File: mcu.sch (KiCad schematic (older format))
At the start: 13 parts, among them P3 SWD, P7 Thumb-Joystick, SW1 SW_PUSH, U3 LCD-2x16, U4 STM32F401xB/C-LQFP

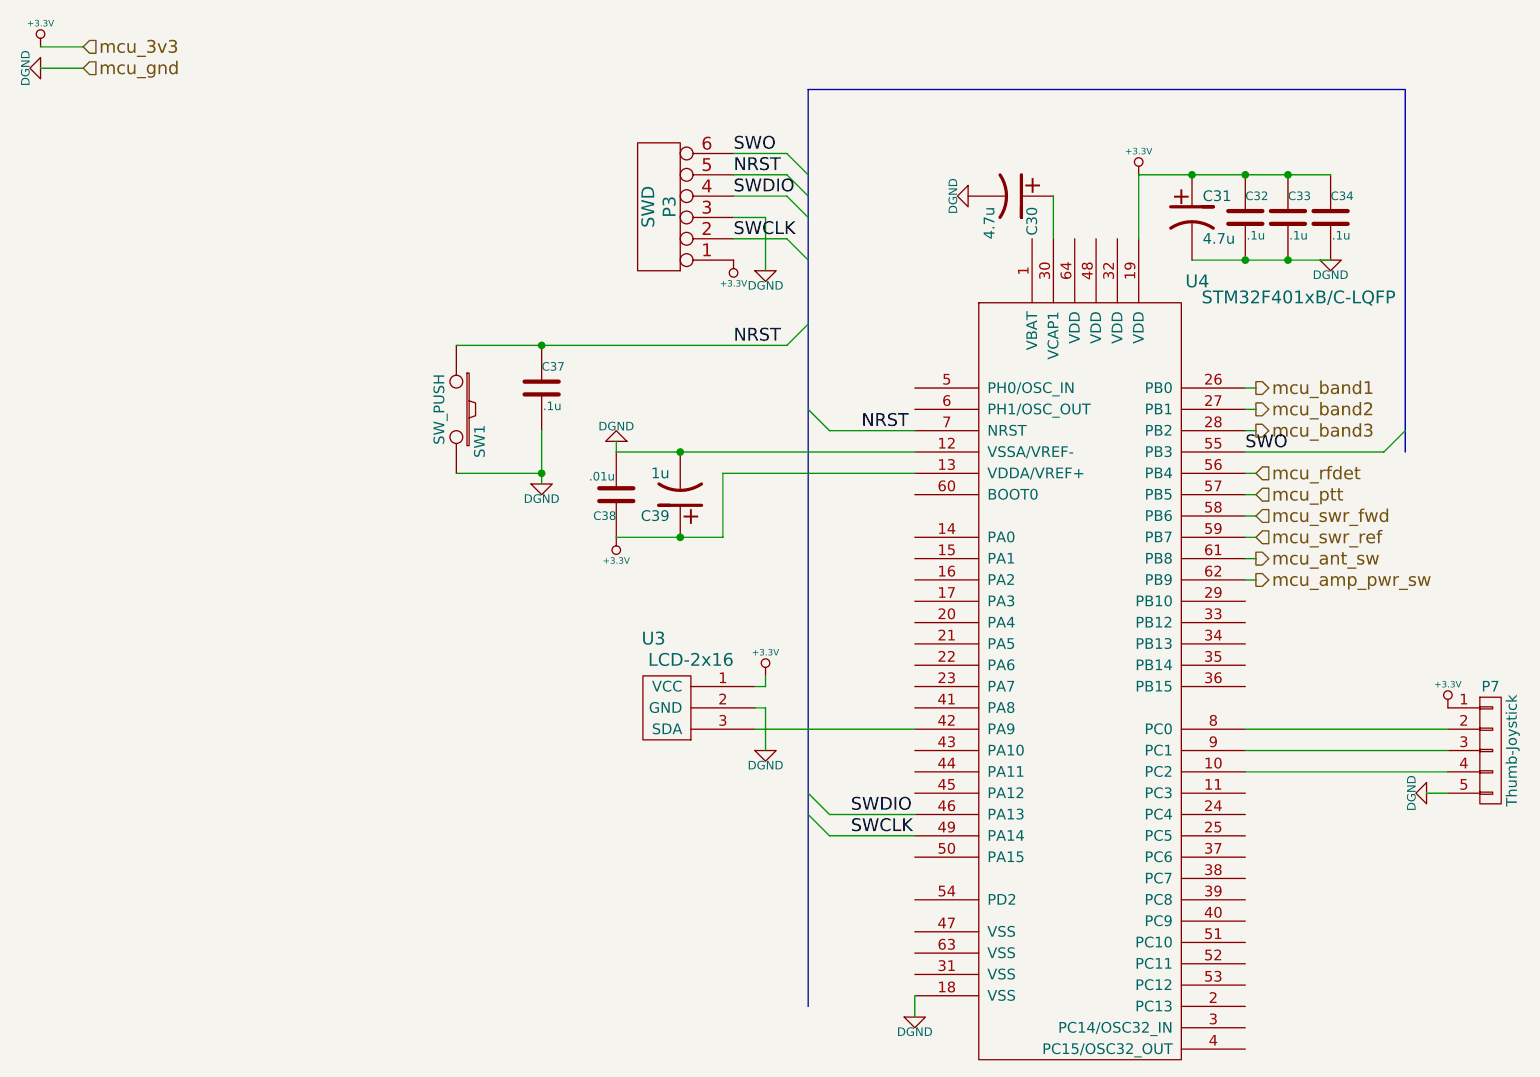
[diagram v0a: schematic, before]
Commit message: All layed out
Several net errors fixed, and some mcu pins reassigned for better layout.
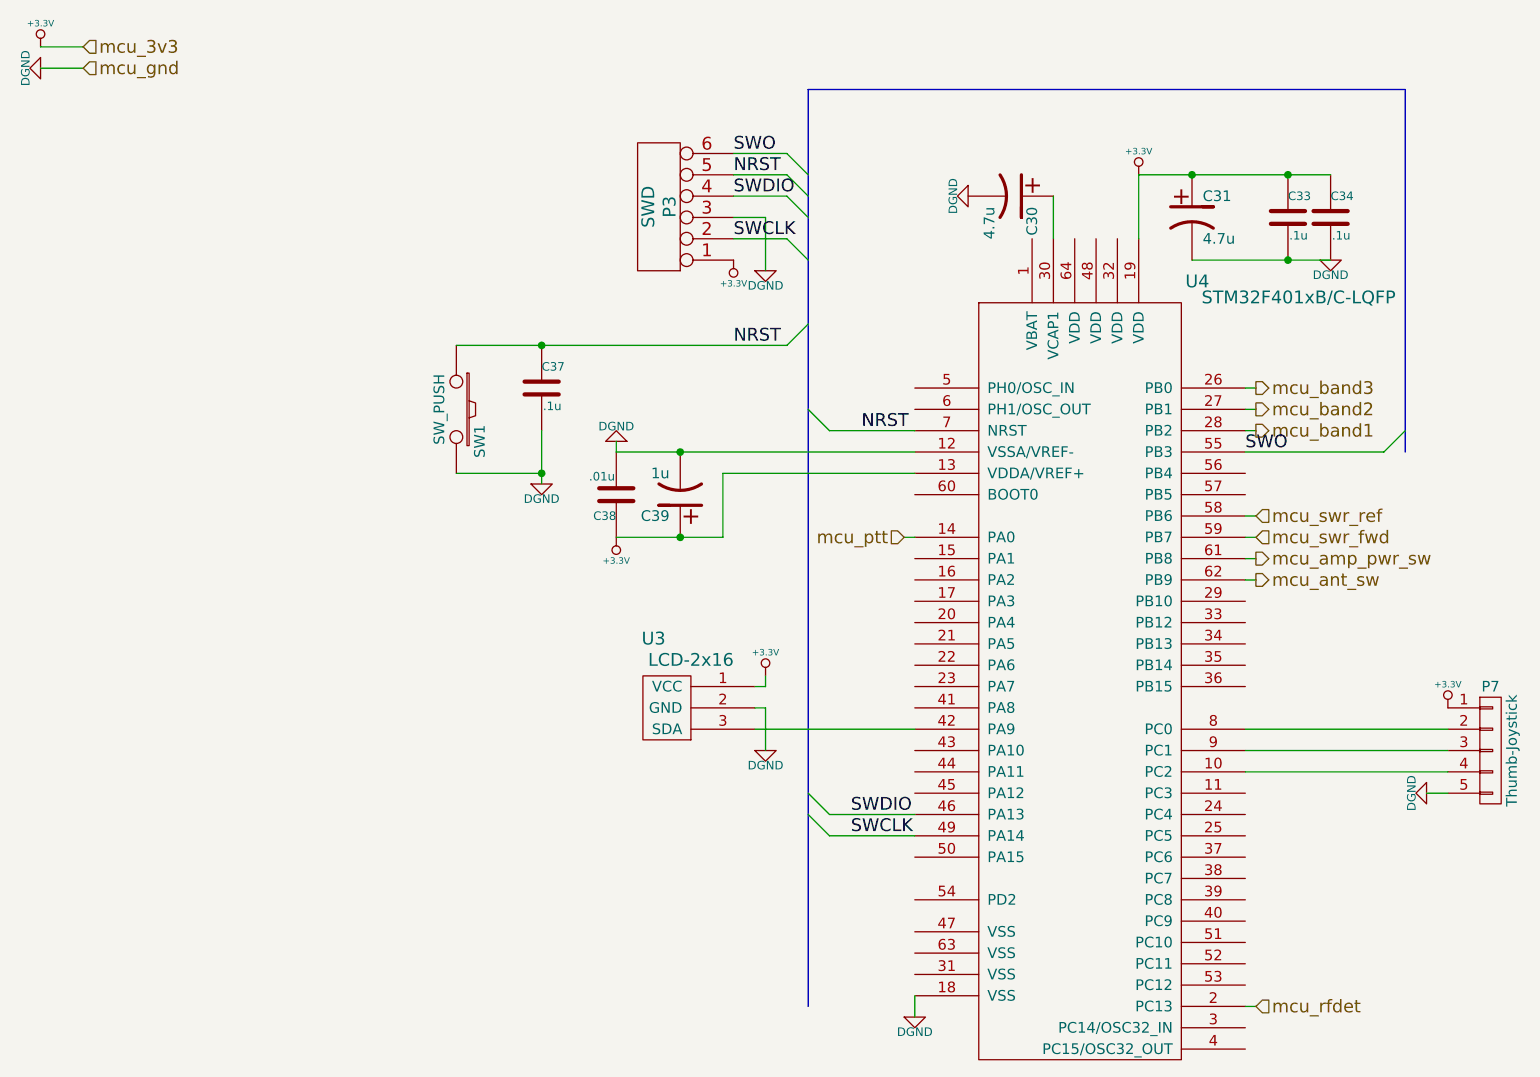
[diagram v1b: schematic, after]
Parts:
- removed C32: .1u, Capacitors_SMD:C_0805_HandSoldering, symbol C
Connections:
- net mcu_amp_pwr_sw: now also U4.61 (PB8); no longer U4.62 (PB9)
- net mcu_ant_sw: now also U4.62 (PB9); no longer U4.61 (PB8)
- net mcu_band1: now also U4.28 (PB2); no longer U4.26 (PB0)
- net mcu_band3: now also U4.26 (PB0); no longer U4.28 (PB2)
- net mcu_ptt: now also U4.14 (PA0); no longer U4.57 (PB5)
- net mcu_rfdet: now also U4.2 (PC13); no longer U4.56 (PB4)
- net mcu_swr_fwd: now also U4.59 (PB7); no longer U4.58 (PB6)
- net mcu_swr_ref: now also U4.58 (PB6); no longer U4.59 (PB7)
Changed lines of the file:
@@
-$EndComp
-$Comp
-L C C32
-U 1 1 547253CC
-P 6450 1600
-F 0 "C32" H 6450 1700 40  0000 L CNN
-F 1 ".1u" H 6456 1515 40  0000 L CNN
-F 2 "Capacitors_SMD:C_0805_HandSoldering" H 6488 1450 30  0001 C CNN
-F 3 "" H 6450 1600 60  0000 C CNN
-	1    6450 1600
-	1    0    0    -1
 $EndComp
 $Comp
@@
 	6200 1800 6850 1800
 Connection ~ 6650 1800
-Connection ~ 6450 1800
 Wire Wire Line
 	5950 1400 6850 1400
 Connection ~ 6650 1400
-Connection ~ 6450 1400
 Wire Wire Line
 	5950 1400 5950 1700
@@
 Wire Wire Line
 	4200 3900 4200 4100
-Text HLabel 6500 2400 2    60   Output ~ 0
+Text HLabel 6500 2600 2    60   Output ~ 0
 mcu_band1
 Text HLabel 6500 2500 2    60   Output ~ 0
 mcu_band2
-Text HLabel 6500 2600 2    60   Output ~ 0
+Text HLabel 6500 2400 2    60   Output ~ 0
 mcu_band3
 Wire Wire Line
@@
 Wire Wire Line
 	6450 2600 6500 2600
-Text HLabel 6500 2800 2    60   Input ~ 0
+Text HLabel 6500 5300 2    60   Input ~ 0
 mcu_rfdet
-Wire Wire Line
-	6450 2800 6500 2800
-Text HLabel 6500 2900 2    60   Input ~ 0
+Text HLabel 4850 3100 0    60   Input ~ 0
 mcu_ptt
-Wire Wire Line
-	6500 2900 6450 2900
+Text HLabel 6500 3100 2    60   Input ~ 0
+mcu_swr_fwd
 Text HLabel 6500 3000 2    60   Input ~ 0
-mcu_swr_fwd
-Text HLabel 6500 3100 2    60   Input ~ 0
 mcu_swr_ref
 Wire Wire Line
@@
 Wire Wire Line
 	6500 3100 6450 3100
+Text HLabel 6500 3300 2    60   Output ~ 0
+mcu_ant_sw
 Text HLabel 6500 3200 2    60   Output ~ 0
-mcu_ant_sw
-Text HLabel 6500 3300 2    60   Output ~ 0
 mcu_amp_pwr_sw
 Wire Wire Line
@@
 	0    1    1    0
 $EndComp
+Wire Wire Line
+	4900 3100 4850 3100
+Wire Wire Line
+	6450 5300 6500 5300
 $EndSCHEMATC

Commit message: Connected all mcu VSS and VDD pins.
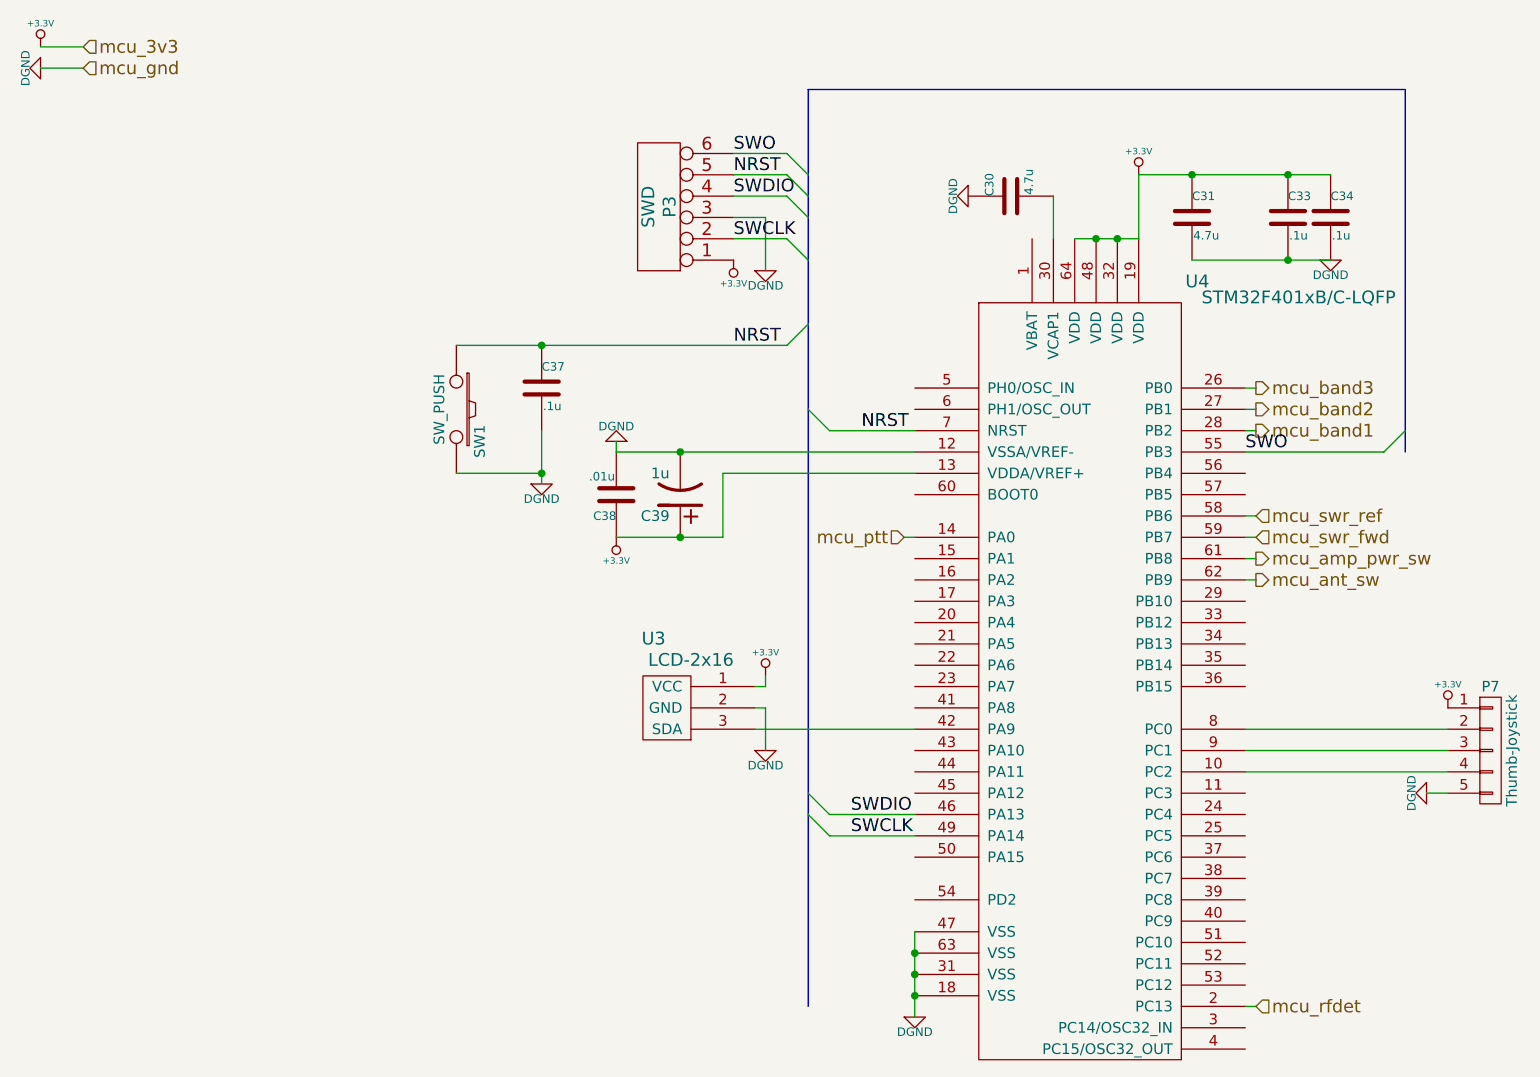
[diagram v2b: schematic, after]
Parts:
- removed C30, C31: 4.7u, Capacitors_ThroughHole:Capacitor5x11RM2.5, symbol CP1
- added C30, C31: 4.7u, Capacitors_SMD:C_0805_HandSoldering, symbol C
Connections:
- net +3.3V: now also U4.32 (VDD), U4.48 (VDD), U4.64 (VDD), C31.1
- net DGND: now also U4.31 (VSS), U4.47 (VSS), U4.63 (VSS), C30.1, C31.2
- net at U4.30 (VCAP1): now also C30.2
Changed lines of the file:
@@
 SWO
-$Comp
-L CP1 C30
-U 1 1 54725387
-P 5350 1500
-F 0 "C30" H 5400 1600 50  0000 L CNN
-F 1 "4.7u" H 5400 1400 50  0000 L CNN
-F 2 "Capacitors_ThroughHole:Capacitor5x11RM2.5" H 5350 1500 60  0001 C CNN
-F 3 "" H 5350 1500 60  0000 C CNN
-	1    5350 1500
-	0    1    1    0
-$EndComp
-$Comp
-L CP1 C31
-U 1 1 547253BF
-P 6200 1600
-F 0 "C31" H 6250 1700 50  0000 L CNN
-F 1 "4.7u" H 6250 1500 50  0000 L CNN
-F 2 "Capacitors_ThroughHole:Capacitor5x11RM2.5" H 6200 1600 60  0001 C CNN
-F 3 "" H 6200 1600 60  0000 C CNN
-	1    6200 1600
-	1    0    0    -1
-$EndComp
 $Comp
 L C C33
@@
 Connection ~ 6650 1400
 Wire Wire Line
-	5950 1400 5950 1700
+	5950 1700 5950 1400
 Connection ~ 6200 1400
 Wire Wire Line
-	4900 5250 4900 5350
+	4900 4950 4900 5350
 Wire Wire Line
 	4050 1600 4200 1600
@@
 Wire Wire Line
 	6450 5300 6500 5300
+Connection ~ 4900 5050
+Connection ~ 4900 5250
+Connection ~ 4900 5150
+Wire Wire Line
+	5650 1700 5950 1700
+Connection ~ 5750 1700
+Connection ~ 5850 1700
+$Comp
+L C C31
+U 1 1 548C5B39
+P 6200 1600
+F 0 "C31" H 6200 1700 40  0000 L CNN
+F 1 "4.7u" H 6206 1515 40  0000 L CNN
+F 2 "Capacitors_SMD:C_0805_HandSoldering" H 6238 1450 30  0001 C CNN
+F 3 "" H 6200 1600 60  0000 C CNN
+	1    6200 1600
+	1    0    0    -1
+$EndComp
+$Comp
+L C C30
+U 1 1 548C5F55
+P 5350 1500
+F 0 "C30" H 5350 1600 40  0000 L CNN
+F 1 "4.7u" H 5356 1415 40  0000 L CNN
+F 2 "Capacitors_SMD:C_0805_HandSoldering" H 5388 1350 30  0001 C CNN
+F 3 "" H 5350 1500 60  0000 C CNN
+	1    5350 1500
+	0    -1   -1   0
+$EndComp
 $EndSCHEMATC
